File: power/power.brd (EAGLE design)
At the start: 62.2 x 53.3 mm, 6 parts

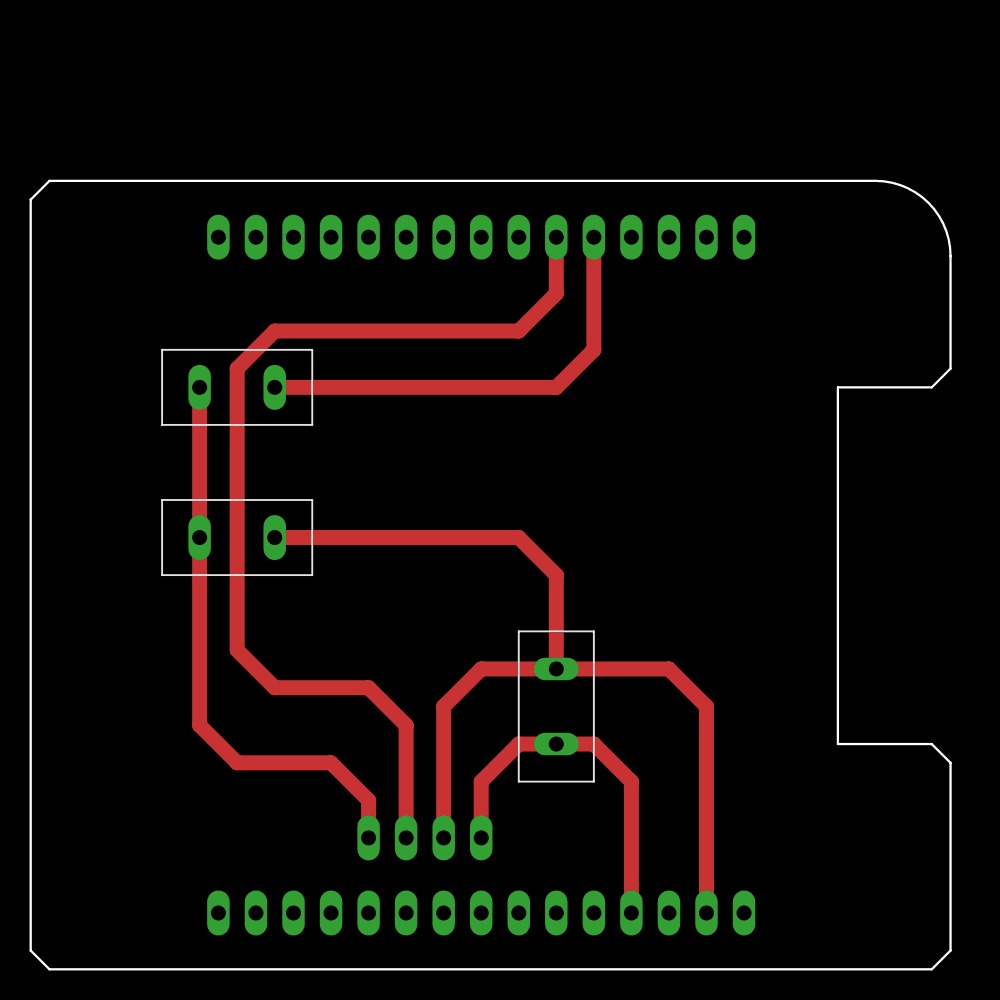
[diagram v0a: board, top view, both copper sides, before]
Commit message: Moved all boards so their bottom left corners are at the origin.
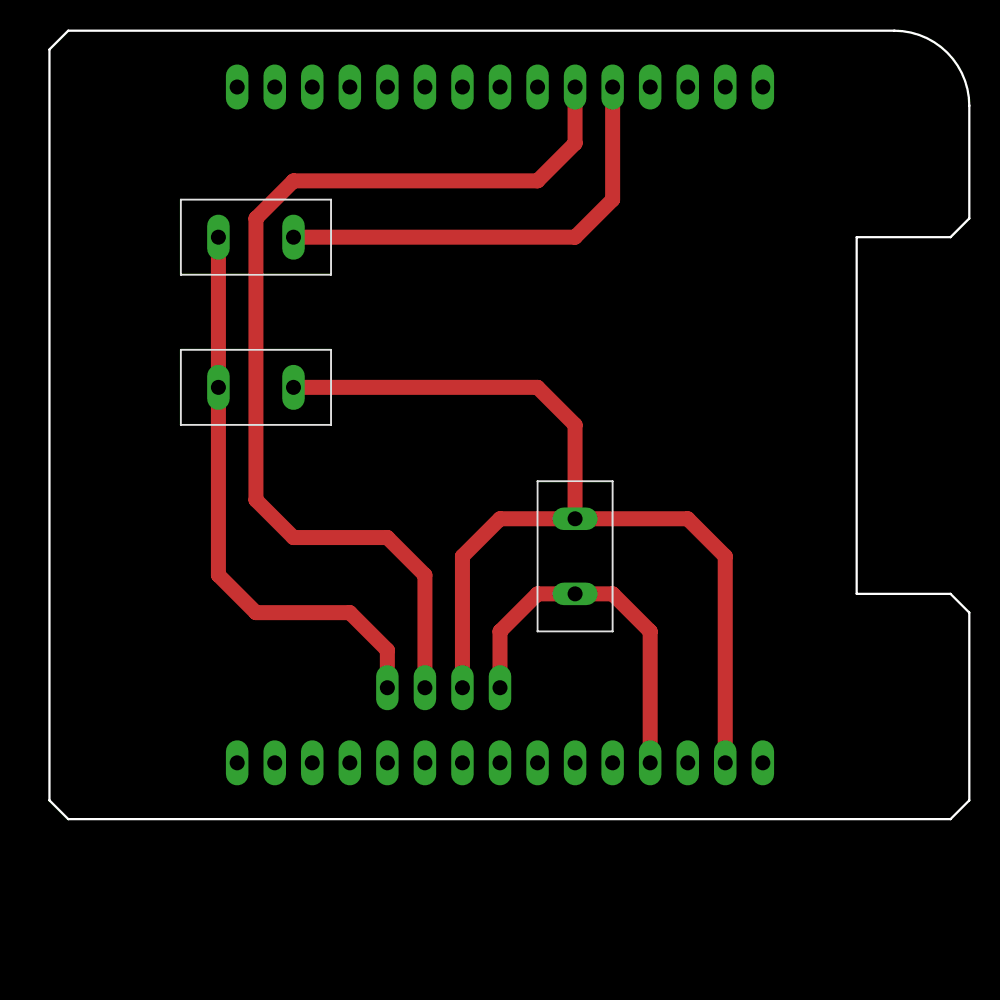
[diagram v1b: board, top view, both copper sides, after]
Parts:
- moved U$1 10.2 mm to (30.5, 49.5)
- moved POWER 10.2 mm to (35.6, 17.8)
- moved U$2 10.2 mm to (30.5, 3.81)
- moved U$4 10.2 mm to (14.0, 29.2)
- moved U$6 10.2 mm to (30.5, 8.89)
- moved U$3 10.2 mm to (14.0, 39.4)
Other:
- outline, holes or cut-outs redrawn
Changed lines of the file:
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@@
 <board>
 <plain>
-<wire x1="53.34" y1="29.21" x2="59.69" y2="29.21" width="0.1524" layer="20"/>
-<wire x1="59.69" y1="29.21" x2="60.96" y2="30.48" width="0.1524" layer="20"/>
-<wire x1="60.96" y1="30.48" x2="60.96" y2="38.1" width="0.1524" layer="20"/>
-<wire x1="60.96" y1="38.1" x2="55.88" y2="43.18" width="0.1524" layer="20" curve="90"/>
-<wire x1="55.88" y1="43.18" x2="0" y2="43.18" width="0.1524" layer="20"/>
-<wire x1="53.34" y1="5.08" x2="53.34" y2="29.21" width="0.1524" layer="20"/>
-<wire x1="53.34" y1="5.08" x2="59.69" y2="5.08" width="0.1524" layer="20"/>
-<wire x1="59.69" y1="5.08" x2="60.96" y2="3.81" width="0.1524" layer="20"/>
-<wire x1="60.96" y1="3.81" x2="60.96" y2="-8.89" width="0.1524" layer="20"/>
-<wire x1="0" y1="43.18" x2="-1.27" y2="41.91" width="0.1524" layer="20"/>
-<wire x1="-1.27" y1="41.91" x2="-1.27" y2="-8.89" width="0.1524" layer="20"/>
-<wire x1="-1.27" y1="-8.89" x2="0" y2="-10.16" width="0.1524" layer="20"/>
-<wire x1="60.96" y1="-8.89" x2="59.69" y2="-10.16" width="0.1524" layer="20"/>
-<wire x1="59.69" y1="-10.16" x2="0" y2="-10.16" width="0.1524" layer="20"/>
+<wire x1="54.61" y1="39.37" x2="60.96" y2="39.37" width="0.1524" layer="20"/>
+<wire x1="60.96" y1="39.37" x2="62.23" y2="40.64" width="0.1524" layer="20"/>
+<wire x1="62.23" y1="40.64" x2="62.23" y2="48.26" width="0.1524" layer="20"/>
+<wire x1="62.23" y1="48.26" x2="57.15" y2="53.34" width="0.1524" layer="20" curve="90"/>
+<wire x1="57.15" y1="53.34" x2="1.27" y2="53.34" width="0.1524" layer="20"/>
+<wire x1="54.61" y1="15.24" x2="54.61" y2="39.37" width="0.1524" layer="20"/>
+<wire x1="54.61" y1="15.24" x2="60.96" y2="15.24" width="0.1524" layer="20"/>
+<wire x1="60.96" y1="15.24" x2="62.23" y2="13.97" width="0.1524" layer="20"/>
+<wire x1="62.23" y1="13.97" x2="62.23" y2="1.27" width="0.1524" layer="20"/>
+<wire x1="1.27" y1="53.34" x2="0" y2="52.07" width="0.1524" layer="20"/>
+<wire x1="0" y1="52.07" x2="0" y2="1.27" width="0.1524" layer="20"/>
+<wire x1="0" y1="1.27" x2="1.27" y2="0" width="0.1524" layer="20"/>
+<wire x1="62.23" y1="1.27" x2="60.96" y2="0" width="0.1524" layer="20"/>
+<wire x1="60.96" y1="0" x2="1.27" y2="0" width="0.1524" layer="20"/>
 </plain>
 <attributes>
@@
 </autorouter>
 <elements>
-<element name="U$1" library="RC Car" package="ARDUINO-NANO-JUMPER-1" value="ARDUINO-NANO-JUMPER-1" x="29.21" y="39.37" smashed="yes"/>
-<element name="U$3" library="RC Car" package="RESISTOR" value="RESISTOR" x="12.7" y="29.21" smashed="yes" rot="R180"/>
-<element name="U$4" library="RC Car" package="RESISTOR" value="RESISTOR" x="12.7" y="19.05" smashed="yes"/>
-<element name="POWER" library="RC Car" package="CAP" value="CAP" x="34.29" y="7.62" smashed="yes" rot="R90"/>
-<element name="U$6" library="RC Car" package="BT" value="BT" x="29.21" y="-1.27" smashed="yes" rot="R180"/>
-<element name="U$2" library="RC Car" package="ARDUINO-NANO-JUMPER-2" value="ARDUINO-NANO-JUMPER-2" x="29.21" y="-6.35" smashed="yes"/>
+<element name="U$1" library="RC Car" package="ARDUINO-NANO-JUMPER-1" value="ARDUINO-NANO-JUMPER-1" x="30.48" y="49.53" smashed="yes"/>
+<element name="U$3" library="RC Car" package="RESISTOR" value="RESISTOR" x="13.97" y="39.37" smashed="yes" rot="R180"/>
+<element name="U$4" library="RC Car" package="RESISTOR" value="RESISTOR" x="13.97" y="29.21" smashed="yes"/>
+<element name="POWER" library="RC Car" package="CAP" value="CAP" x="35.56" y="17.78" smashed="yes" rot="R90"/>
+<element name="U$6" library="RC Car" package="BT" value="BT" x="30.48" y="8.89" smashed="yes" rot="R180"/>
+<element name="U$2" library="RC Car" package="ARDUINO-NANO-JUMPER-2" value="ARDUINO-NANO-JUMPER-2" x="30.48" y="3.81" smashed="yes"/>
 </elements>
 <signals>
@@
 <contactref element="U$4" pad="POS"/>
 <contactref element="U$6" pad="RXD"/>
-<wire x1="10.16" y1="29.21" x2="10.16" y2="19.05" width="1.016" layer="1"/>
-<wire x1="21.59" y1="-1.27" x2="21.59" y2="1.27" width="1.016" layer="1"/>
-<wire x1="21.59" y1="1.27" x2="19.05" y2="3.81" width="1.016" layer="1"/>
-<wire x1="19.05" y1="3.81" x2="12.7" y2="3.81" width="1.016" layer="1"/>
-<wire x1="12.7" y1="3.81" x2="10.16" y2="6.35" width="1.016" layer="1"/>
-<wire x1="10.16" y1="6.35" x2="10.16" y2="19.05" width="1.016" layer="1"/>
+<wire x1="11.43" y1="39.37" x2="11.43" y2="29.21" width="1.016" layer="1"/>
+<wire x1="22.86" y1="8.89" x2="22.86" y2="11.43" width="1.016" layer="1"/>
+<wire x1="22.86" y1="11.43" x2="20.32" y2="13.97" width="1.016" layer="1"/>
+<wire x1="20.32" y1="13.97" x2="13.97" y2="13.97" width="1.016" layer="1"/>
+<wire x1="13.97" y1="13.97" x2="11.43" y2="16.51" width="1.016" layer="1"/>
+<wire x1="11.43" y1="16.51" x2="11.43" y2="29.21" width="1.016" layer="1"/>
 </signal>
 <signal name="D02">
 <contactref element="U$1" pad="D2"/>
 <contactref element="U$3" pad="POS"/>
-<wire x1="36.83" y1="39.37" x2="36.83" y2="31.75" width="1.016" layer="1"/>
-<wire x1="36.83" y1="31.75" x2="34.29" y2="29.21" width="1.016" layer="1"/>
-<wire x1="34.29" y1="29.21" x2="15.24" y2="29.21" width="1.016" layer="1"/>
+<wire x1="38.1" y1="49.53" x2="38.1" y2="41.91" width="1.016" layer="1"/>
+<wire x1="38.1" y1="41.91" x2="35.56" y2="39.37" width="1.016" layer="1"/>
+<wire x1="35.56" y1="39.37" x2="16.51" y2="39.37" width="1.016" layer="1"/>
 </signal>
 <signal name="D03">
 <contactref element="U$6" pad="TXD"/>
 <contactref element="U$1" pad="D3"/>
-<wire x1="21.59" y1="8.89" x2="15.24" y2="8.89" width="1.016" layer="1"/>
-<wire x1="15.24" y1="8.89" x2="12.7" y2="11.43" width="1.016" layer="1"/>
-<wire x1="12.7" y1="11.43" x2="12.7" y2="30.48" width="1.016" layer="1"/>
-<wire x1="12.7" y1="30.48" x2="15.24" y2="33.02" width="1.016" layer="1"/>
-<wire x1="15.24" y1="33.02" x2="31.75" y2="33.02" width="1.016" layer="1"/>
-<wire x1="31.75" y1="33.02" x2="34.29" y2="35.56" width="1.016" layer="1"/>
-<wire x1="34.29" y1="35.56" x2="34.29" y2="39.37" width="1.016" layer="1"/>
-<wire x1="24.13" y1="-1.27" x2="24.13" y2="6.35" width="1.016" layer="1"/>
-<wire x1="24.13" y1="6.35" x2="21.59" y2="8.89" width="1.016" layer="1"/>
+<wire x1="22.86" y1="19.05" x2="16.51" y2="19.05" width="1.016" layer="1"/>
+<wire x1="16.51" y1="19.05" x2="13.97" y2="21.59" width="1.016" layer="1"/>
+<wire x1="13.97" y1="21.59" x2="13.97" y2="40.64" width="1.016" layer="1"/>
+<wire x1="13.97" y1="40.64" x2="16.51" y2="43.18" width="1.016" layer="1"/>
+<wire x1="16.51" y1="43.18" x2="33.02" y2="43.18" width="1.016" layer="1"/>
+<wire x1="33.02" y1="43.18" x2="35.56" y2="45.72" width="1.016" layer="1"/>
+<wire x1="35.56" y1="45.72" x2="35.56" y2="49.53" width="1.016" layer="1"/>
+<wire x1="25.4" y1="8.89" x2="25.4" y2="16.51" width="1.016" layer="1"/>
+<wire x1="25.4" y1="16.51" x2="22.86" y2="19.05" width="1.016" layer="1"/>
 </signal>
 <signal name="GND">
@@
 <contactref element="U$6" pad="GND"/>
 <contactref element="U$2" pad="GND"/>
-<wire x1="34.29" y1="10.16" x2="34.29" y2="16.51" width="1.016" layer="1"/>
-<wire x1="34.29" y1="16.51" x2="31.75" y2="19.05" width="1.016" layer="1"/>
-<wire x1="31.75" y1="19.05" x2="15.24" y2="19.05" width="1.016" layer="1"/>
-<wire x1="34.29" y1="10.16" x2="29.21" y2="10.16" width="1.016" layer="1"/>
-<wire x1="29.21" y1="10.16" x2="26.67" y2="7.62" width="1.016" layer="1"/>
-<wire x1="26.67" y1="7.62" x2="26.67" y2="-1.27" width="1.016" layer="1"/>
-<wire x1="44.45" y1="-6.35" x2="44.45" y2="7.62" width="1.016" layer="1"/>
-<wire x1="44.45" y1="7.62" x2="41.91" y2="10.16" width="1.016" layer="1"/>
-<wire x1="41.91" y1="10.16" x2="34.29" y2="10.16" width="1.016" layer="1"/>
+<wire x1="35.56" y1="20.32" x2="35.56" y2="26.67" width="1.016" layer="1"/>
+<wire x1="35.56" y1="26.67" x2="33.02" y2="29.21" width="1.016" layer="1"/>
+<wire x1="33.02" y1="29.21" x2="16.51" y2="29.21" width="1.016" layer="1"/>
+<wire x1="35.56" y1="20.32" x2="30.48" y2="20.32" width="1.016" layer="1"/>
+<wire x1="30.48" y1="20.32" x2="27.94" y2="17.78" width="1.016" layer="1"/>
+<wire x1="27.94" y1="17.78" x2="27.94" y2="8.89" width="1.016" layer="1"/>
+<wire x1="45.72" y1="3.81" x2="45.72" y2="17.78" width="1.016" layer="1"/>
+<wire x1="45.72" y1="17.78" x2="43.18" y2="20.32" width="1.016" layer="1"/>
+<wire x1="43.18" y1="20.32" x2="35.56" y2="20.32" width="1.016" layer="1"/>
 </signal>
 <signal name="5V">
@@
 <contactref element="U$6" pad="VCC"/>
 <contactref element="U$2" pad="5V"/>
-<wire x1="34.29" y1="5.08" x2="31.75" y2="5.08" width="1.016" layer="1"/>
-<wire x1="31.75" y1="5.08" x2="29.21" y2="2.54" width="1.016" layer="1"/>
-<wire x1="29.21" y1="2.54" x2="29.21" y2="-1.27" width="1.016" layer="1"/>
-<wire x1="39.37" y1="-6.35" x2="39.37" y2="2.54" width="1.016" layer="1"/>
-<wire x1="39.37" y1="2.54" x2="36.83" y2="5.08" width="1.016" layer="1"/>
-<wire x1="36.83" y1="5.08" x2="34.29" y2="5.08" width="1.016" layer="1"/>
+<wire x1="35.56" y1="15.24" x2="33.02" y2="15.24" width="1.016" layer="1"/>
+<wire x1="33.02" y1="15.24" x2="30.48" y2="12.7" width="1.016" layer="1"/>
+<wire x1="30.48" y1="12.7" x2="30.48" y2="8.89" width="1.016" layer="1"/>
+<wire x1="40.64" y1="3.81" x2="40.64" y2="12.7" width="1.016" layer="1"/>
+<wire x1="40.64" y1="12.7" x2="38.1" y2="15.24" width="1.016" layer="1"/>
+<wire x1="38.1" y1="15.24" x2="35.56" y2="15.24" width="1.016" layer="1"/>
 </signal>
 </signals>

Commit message: Fixed board lengths for motor and power boards.
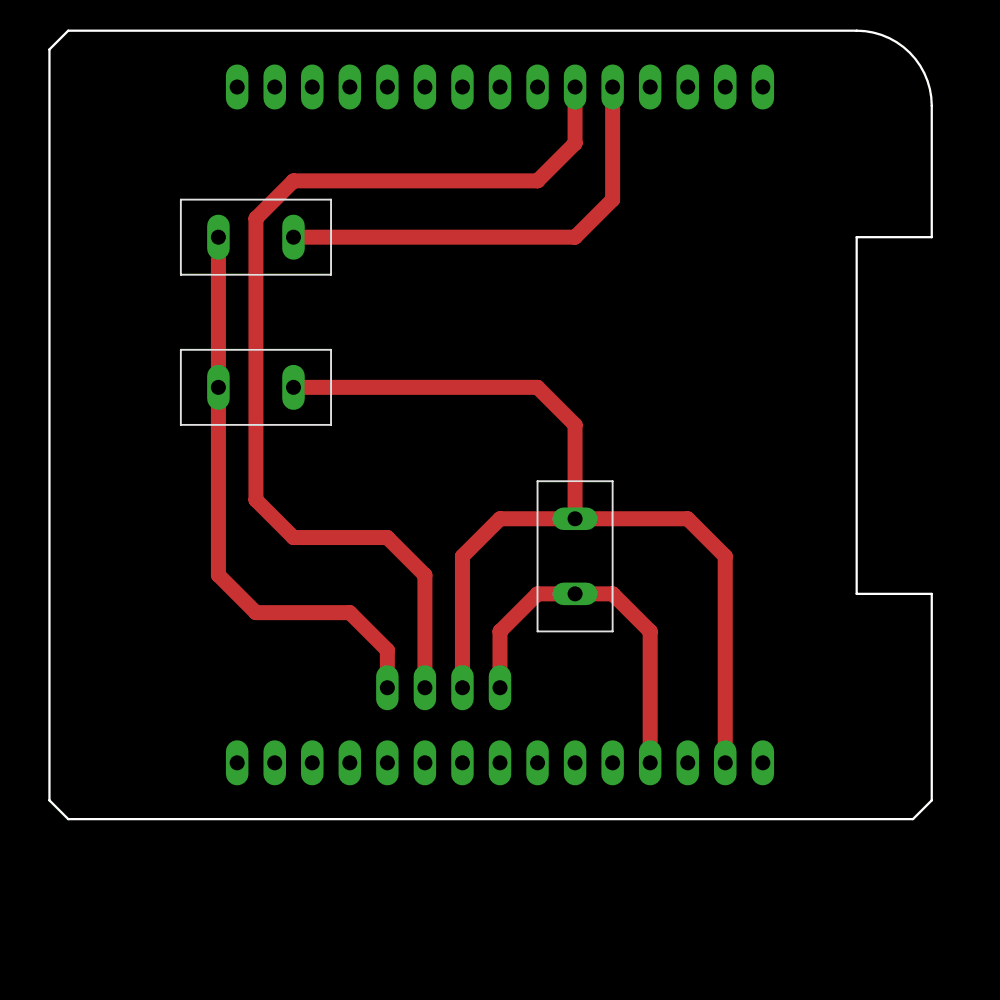
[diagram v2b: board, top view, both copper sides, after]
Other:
- board size 62.2 x 53.3 mm -> 59.7 x 53.3 mm
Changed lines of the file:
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@@
 <board>
 <plain>
-<wire x1="54.61" y1="39.37" x2="60.96" y2="39.37" width="0.1524" layer="20"/>
-<wire x1="60.96" y1="39.37" x2="62.23" y2="40.64" width="0.1524" layer="20"/>
-<wire x1="62.23" y1="40.64" x2="62.23" y2="48.26" width="0.1524" layer="20"/>
-<wire x1="62.23" y1="48.26" x2="57.15" y2="53.34" width="0.1524" layer="20" curve="90"/>
-<wire x1="57.15" y1="53.34" x2="1.27" y2="53.34" width="0.1524" layer="20"/>
+<wire x1="54.61" y1="39.37" x2="59.69" y2="39.37" width="0.1524" layer="20"/>
+<wire x1="59.69" y1="39.37" x2="59.69" y2="48.26" width="0.1524" layer="20"/>
+<wire x1="59.69" y1="48.26" x2="54.61" y2="53.34" width="0.1524" layer="20" curve="90"/>
+<wire x1="54.61" y1="53.34" x2="1.27" y2="53.34" width="0.1524" layer="20"/>
 <wire x1="54.61" y1="15.24" x2="54.61" y2="39.37" width="0.1524" layer="20"/>
-<wire x1="54.61" y1="15.24" x2="60.96" y2="15.24" width="0.1524" layer="20"/>
-<wire x1="60.96" y1="15.24" x2="62.23" y2="13.97" width="0.1524" layer="20"/>
-<wire x1="62.23" y1="13.97" x2="62.23" y2="1.27" width="0.1524" layer="20"/>
+<wire x1="54.61" y1="15.24" x2="59.69" y2="15.24" width="0.1524" layer="20"/>
+<wire x1="59.69" y1="15.24" x2="59.69" y2="1.27" width="0.1524" layer="20"/>
+<wire x1="59.69" y1="1.27" x2="58.42" y2="0" width="0.1524" layer="20"/>
+<wire x1="58.42" y1="0" x2="1.27" y2="0" width="0.1524" layer="20"/>
 <wire x1="1.27" y1="53.34" x2="0" y2="52.07" width="0.1524" layer="20"/>
 <wire x1="0" y1="52.07" x2="0" y2="1.27" width="0.1524" layer="20"/>
 <wire x1="0" y1="1.27" x2="1.27" y2="0" width="0.1524" layer="20"/>
-<wire x1="62.23" y1="1.27" x2="60.96" y2="0" width="0.1524" layer="20"/>
-<wire x1="60.96" y1="0" x2="1.27" y2="0" width="0.1524" layer="20"/>
 </plain>
 <attributes>
